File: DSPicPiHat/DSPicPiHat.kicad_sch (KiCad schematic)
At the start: 20 parts

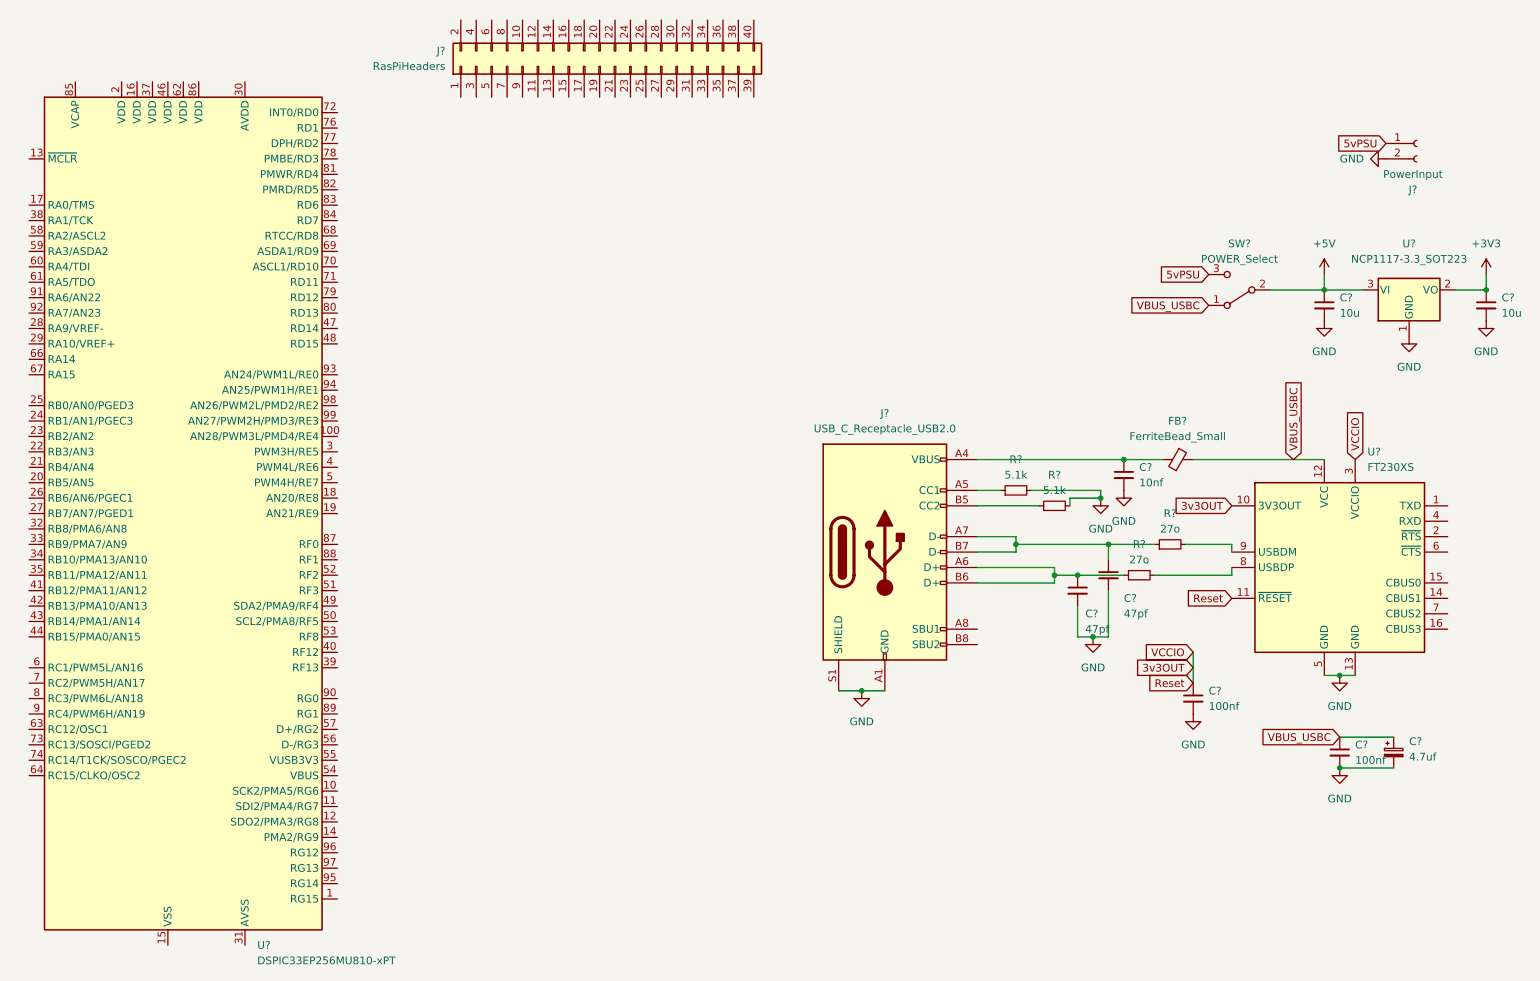
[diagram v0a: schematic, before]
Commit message: Added debug port, polyfuse, and organizational changes.
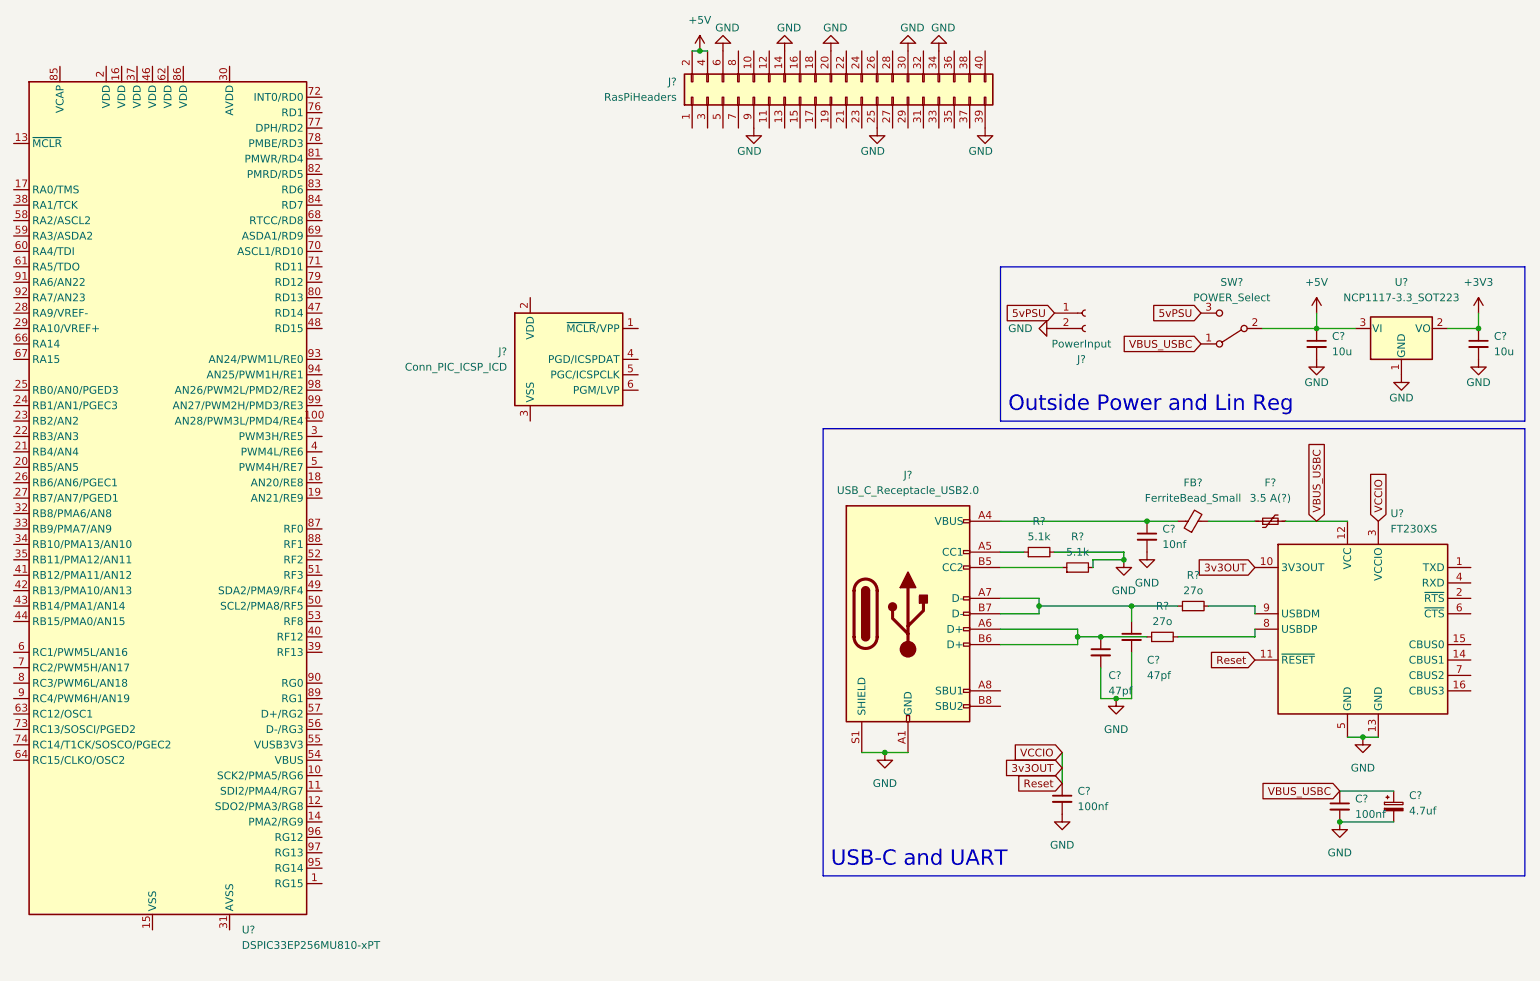
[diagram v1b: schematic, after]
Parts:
- added F?: 3.5 A(?), symbol Device:Polyfuse_Small
- added J?: Conn_PIC_ICSP_ICD, symbol Connector:Conn_PIC_ICSP_ICD
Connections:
- net +5V: now also J?.2 (Pin_2), J?.4 (Pin_4)
- net GND: now also J?.14 (Pin_14), J?.20 (Pin_20), J?.25 (Pin_25), J?.30 (Pin_30), J?.34 (Pin_34), J?.39 (Pin_39), J?.6 (Pin_6), J?.9 (Pin_9)
- net VBUS_USBC: now also F?.2; no longer FB?.2
- new net: F?.1, FB?.2
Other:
- note added: "Outside Power and Lin Reg"
- note added: "USB-C and UART"
- moved on the sheet: C?, FB?, J?, R?, SW?, U?

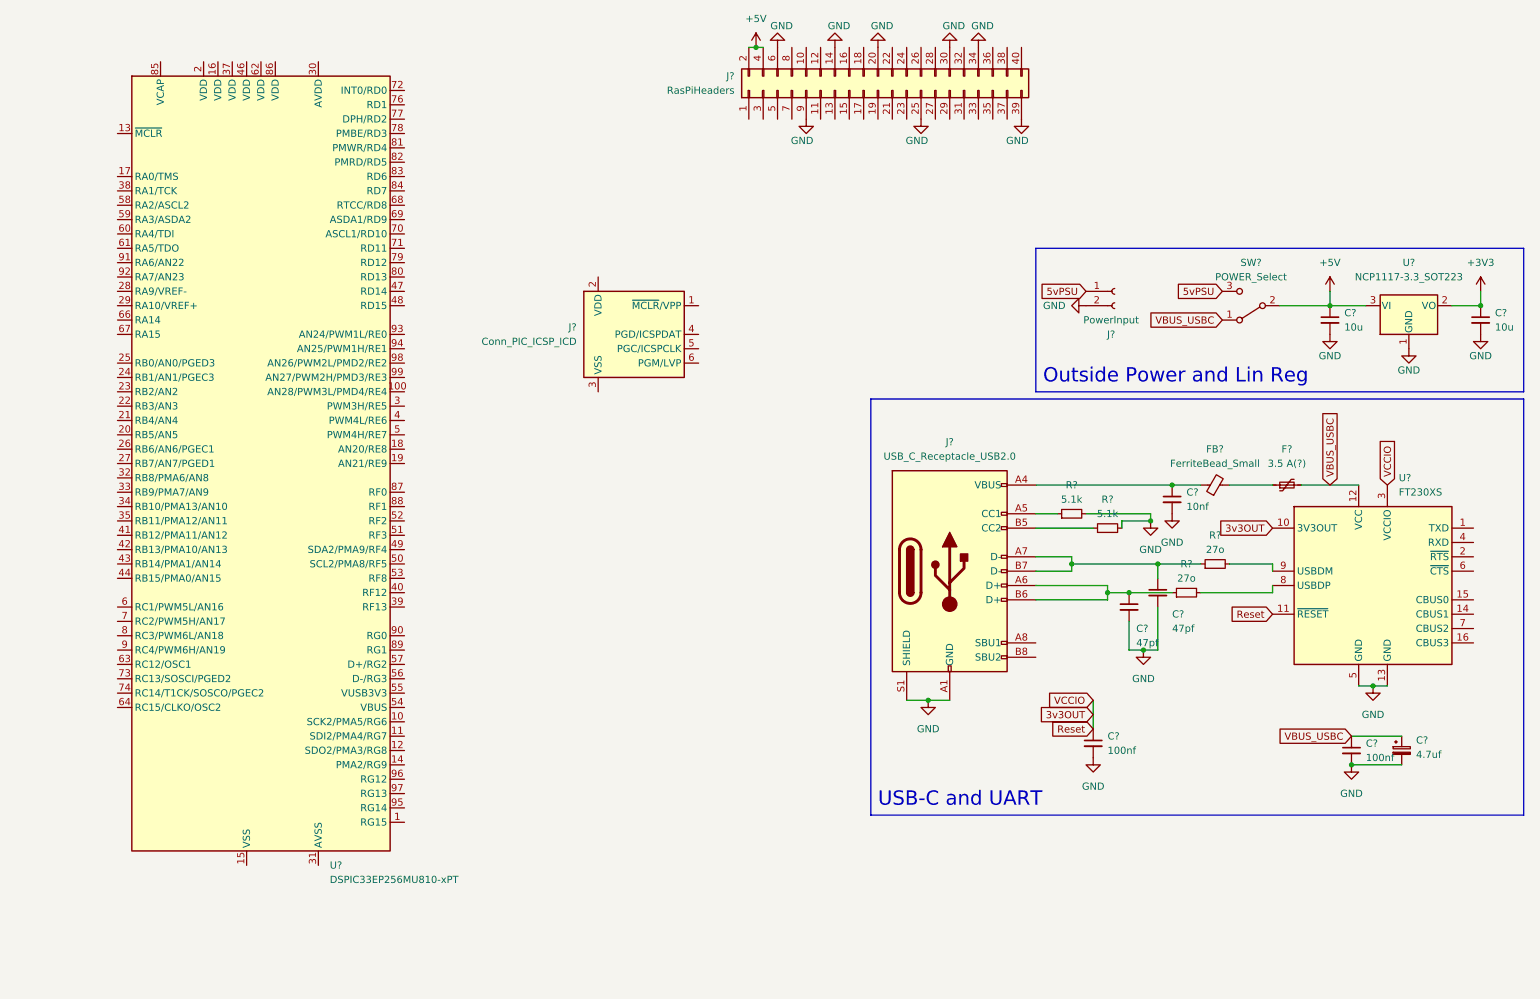
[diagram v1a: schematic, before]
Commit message: Added correct dsPIC chip and connected it to parts., added coil driver connector, added tvs diodes.
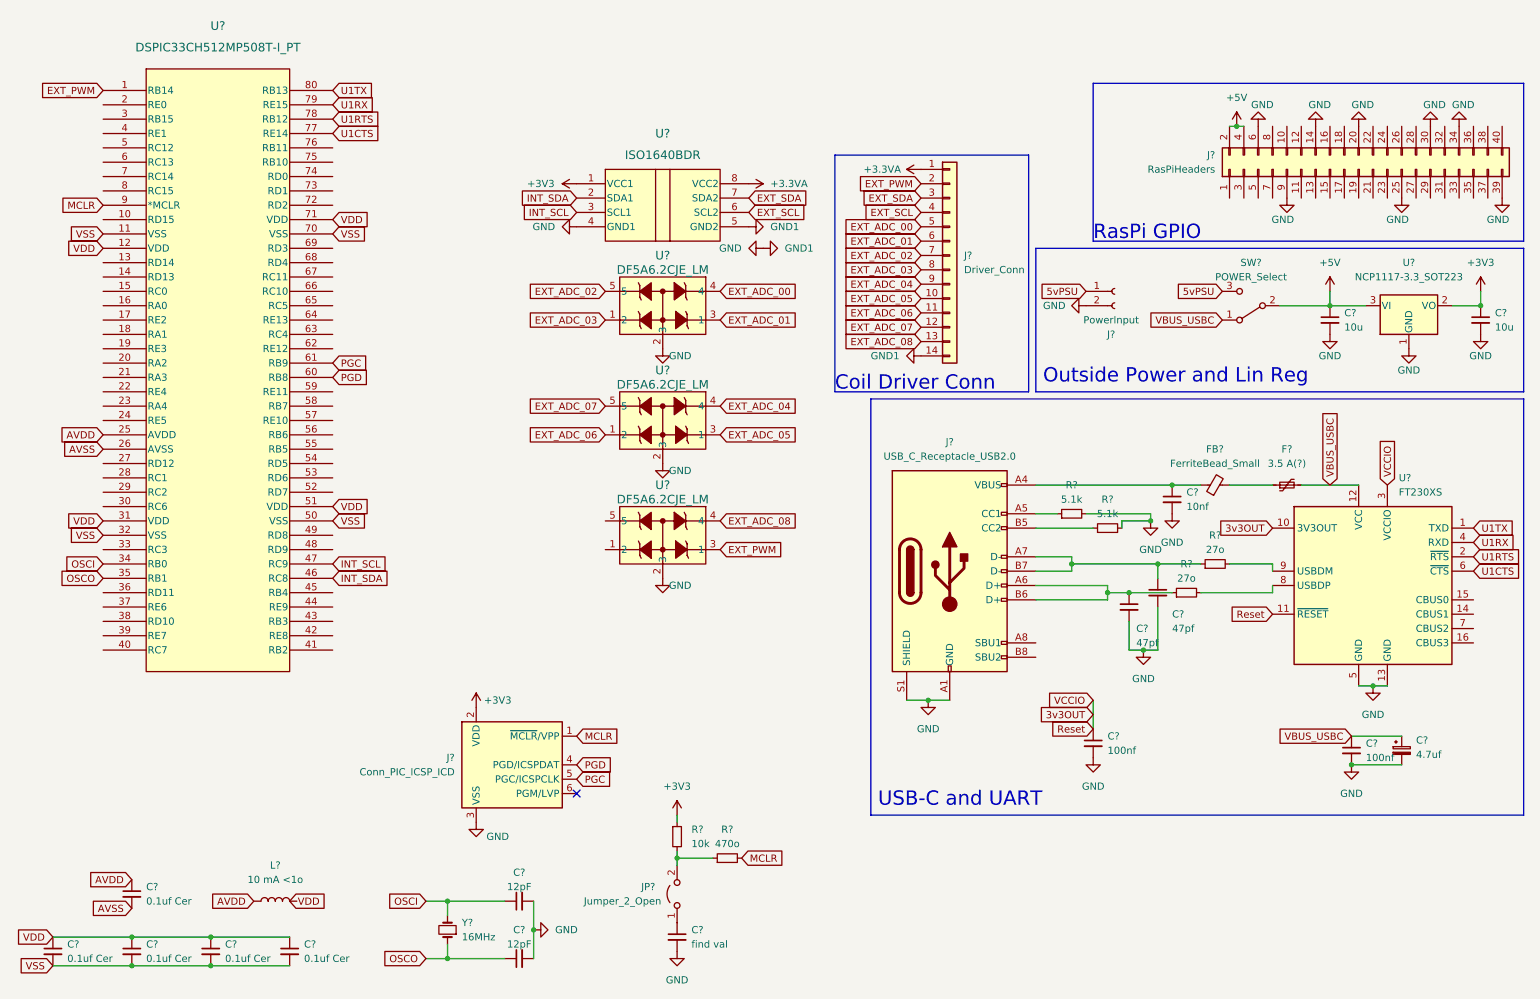
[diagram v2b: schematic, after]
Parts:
- removed U?: DSPIC33EP256MU810-xPT, Package_QFP:TQFP-100_14x14mm_P0.5mm, symbol DSP_Microchip_DSPIC33:DSPIC33EP256MU810-xPT
- added C? (x5): 0.1uf Cer, symbol Device:C_Small
- added C? (x2): 12pF, symbol Device:C_Small
- added C?: find val, symbol Device:C_Small
- added J?: Driver_Conn, symbol Connector_Generic:Conn_01x14
- added JP?: Jumper_2_Open, symbol Jumper:Jumper_2_Open
- added L?: 10 mA <1o, symbol Device:L
- added R?: 470o, symbol Device:R_Small
- added R?: 10k, symbol Device:R_Small
- added U?: ISO1640BDR, D0008B-IPC_A, symbol PiHatLib:ISO1640BDR
- added U? (x3): DF5A6.2CJE_LM, SOT-553 ESV_TOS, symbol PiHatLib:DF5A6.2CJE_LM
- added U?: DSPIC33CH512MP508T-I_PT, TQFP80_12x12MC_MCH, symbol PiHatLib:DSPIC33CH512MP508T-I_PT
- added Y?: 16MHz, symbol Device:Crystal_Small
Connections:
- net +3V3: now also J?.2 (VDD), R?.1, U?.1 (VCC1)
- net GND: now also J?.3 (VSS), C?.2, C?.2, C?.2, J?.14 (Pin_14), U?.2 (3), U?.2 (3), U?.2 (3), U?.4 (GND1), U?.5 (GND2)
- net MCLR: now reaches J?.1 (~{MCLR}/VPP)
- net MCLR: now also R?.2, U?.9 (*MCLR)
- net PGD: now reaches J?.4 (PGD/ICSPDAT)
- net PGD: now also U?.60 (RB8)
- net PGC: now reaches J?.5 (PGC/ICSPCLK)
- net PGC: now also U?.61 (RB9)
- net U1TX: now reaches U?.1 (TXD)
- net U1TX: now also U?.80 (RB13)
- net U1RTS: now reaches U?.2 (~{RTS})
- net U1RTS: now also U?.78 (RB12)
- net U1RX: now reaches U?.4 (RXD)
- net U1RX: now also U?.79 (RE15)
- net U1CTS: now reaches U?.6 (~{CTS})
- net U1CTS: now also U?.77 (RE14)
- new net: C?.1, JP?.1 (A)
- new net: JP?.2 (B), R?.1, R?.2
- new net +3.3VA: J?.1 (Pin_1), U?.8 (VCC2)
- new net AVDD: C?.1, L?.1, U?.25 (AVDD)
- new net AVSS: C?.2, U?.26 (AVSS)
- new net EXT_ADC_00: J?.5 (Pin_5), U?.4
- new net EXT_ADC_01: J?.6 (Pin_6), U?.3 (1)
- new net EXT_ADC_02: J?.7 (Pin_7), U?.5
- new net EXT_ADC_03: J?.8 (Pin_8), U?.1 (2)
- new net EXT_ADC_04: J?.9 (Pin_9), U?.4
- new net EXT_ADC_05: J?.10 (Pin_10), U?.3 (1)
- new net EXT_ADC_06: J?.11 (Pin_11), U?.1 (2)
- new net EXT_ADC_07: J?.12 (Pin_12), U?.5
- new net EXT_ADC_08: J?.13 (Pin_13), U?.4
- new net EXT_PWM: J?.2 (Pin_2), U?.1 (RB14), U?.3 (1)
- new net EXT_SCL: J?.4 (Pin_4), U?.6 (SCL2)
- new net EXT_SDA: J?.3 (Pin_3), U?.7 (SDA2)
- new net INT_SCL: U?.3 (SCL1), U?.47 (RC9)
- new net INT_SDA: U?.2 (SDA1), U?.46 (RC8)
- new net OSCI: C?.1, U?.34 (RB0), Y?.2
- new net OSCO: C?.1, U?.35 (RB1), Y?.1
- new net VDD: C?.1, C?.1, C?.1, C?.1, U?.12 (VDD), U?.31 (VDD), U?.51 (VDD), U?.71 (VDD)
- new net VSS: C?.2, C?.2, C?.2, C?.2, U?.11 (VSS), U?.32 (VSS), U?.50 (VSS), U?.70 (VSS)
- no-connect marks 0 -> 1
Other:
- note added: "Coil Driver Conn"
- note added: "RasPi GPIO"
- moved on the sheet: J?
